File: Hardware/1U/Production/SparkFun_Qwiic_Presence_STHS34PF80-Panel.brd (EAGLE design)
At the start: 149.1 x 143.3 mm, 1306 parts, among them J1 Qwiic, J10 Qwiic, J11 Qwiic, J13 Qwiic, J14 Qwiic, J16 Qwiic, J17 Qwiic, J19 Qwiic, J2 Qwiic, J20 Qwiic, J22 Qwiic, J23 Qwiic, J25 Qwiic, J26 Qwiic, J28 Qwiic, J29 Qwiic, J31 Qwiic, J32 Qwiic, J34 Qwiic, J35 Qwiic, J37 Qwiic, J38 Qwiic, J4 Qwiic, J40 Qwiic, J41 Qwiic, J43 Qwiic, J44 Qwiic, J46 Qwiic, J47 Qwiic, J49 Qwiic, J5 Qwiic, J50 Qwiic, J52 Qwiic, J53 Qwiic, J55 Qwiic, J56 Qwiic, J58 Qwiic, J59 Qwiic, J61 Qwiic, J62 Qwiic, J64 Qwiic, J65 Qwiic, J67 Qwiic, J68 Qwiic, J7 Qwiic, J70 Qwiic, J71 Qwiic, J73 Qwiic, J74 Qwiic, J8 Qwiic, U1 STHS34PF80, U10 STHS34PF80, U11 STHS34PF80, U12 STHS34PF80, U13 STHS34PF80, U14 STHS34PF80, U15 STHS34PF80, U16 STHS34PF80, U17 STHS34PF80, U18 STHS34PF80, U19 STHS34PF80, U2 STHS34PF80, U20 STHS34PF80, U21 STHS34PF80, U22 STHS34PF80, U23 STHS34PF80, U24 STHS34PF80, U25 STHS34PF80, U3 STHS34PF80, U4 STHS34PF80, U5 STHS34PF80, U6 STHS34PF80, U7 STHS34PF80, U8 STHS34PF80, U9 STHS34PF80

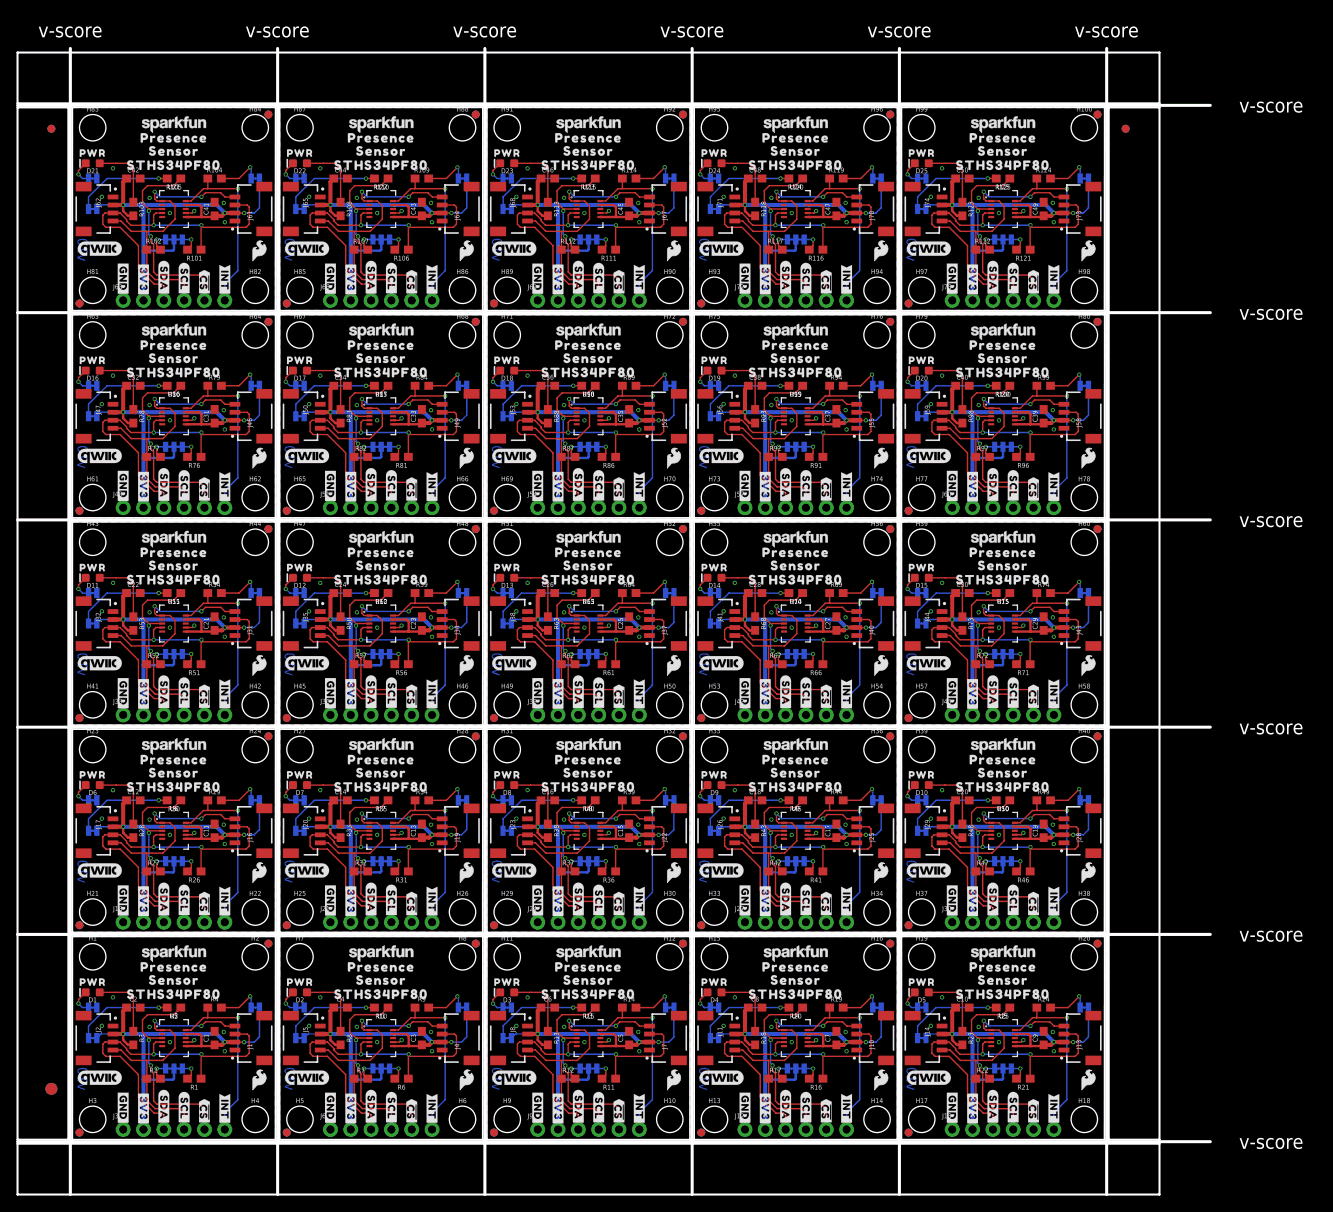
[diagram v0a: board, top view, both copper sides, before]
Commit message: Updated 1U to correct paste layer for main IC
Updated the board and the panel/gerbers to have the correct percentage of fill for the solder paste on the STHS34PF80
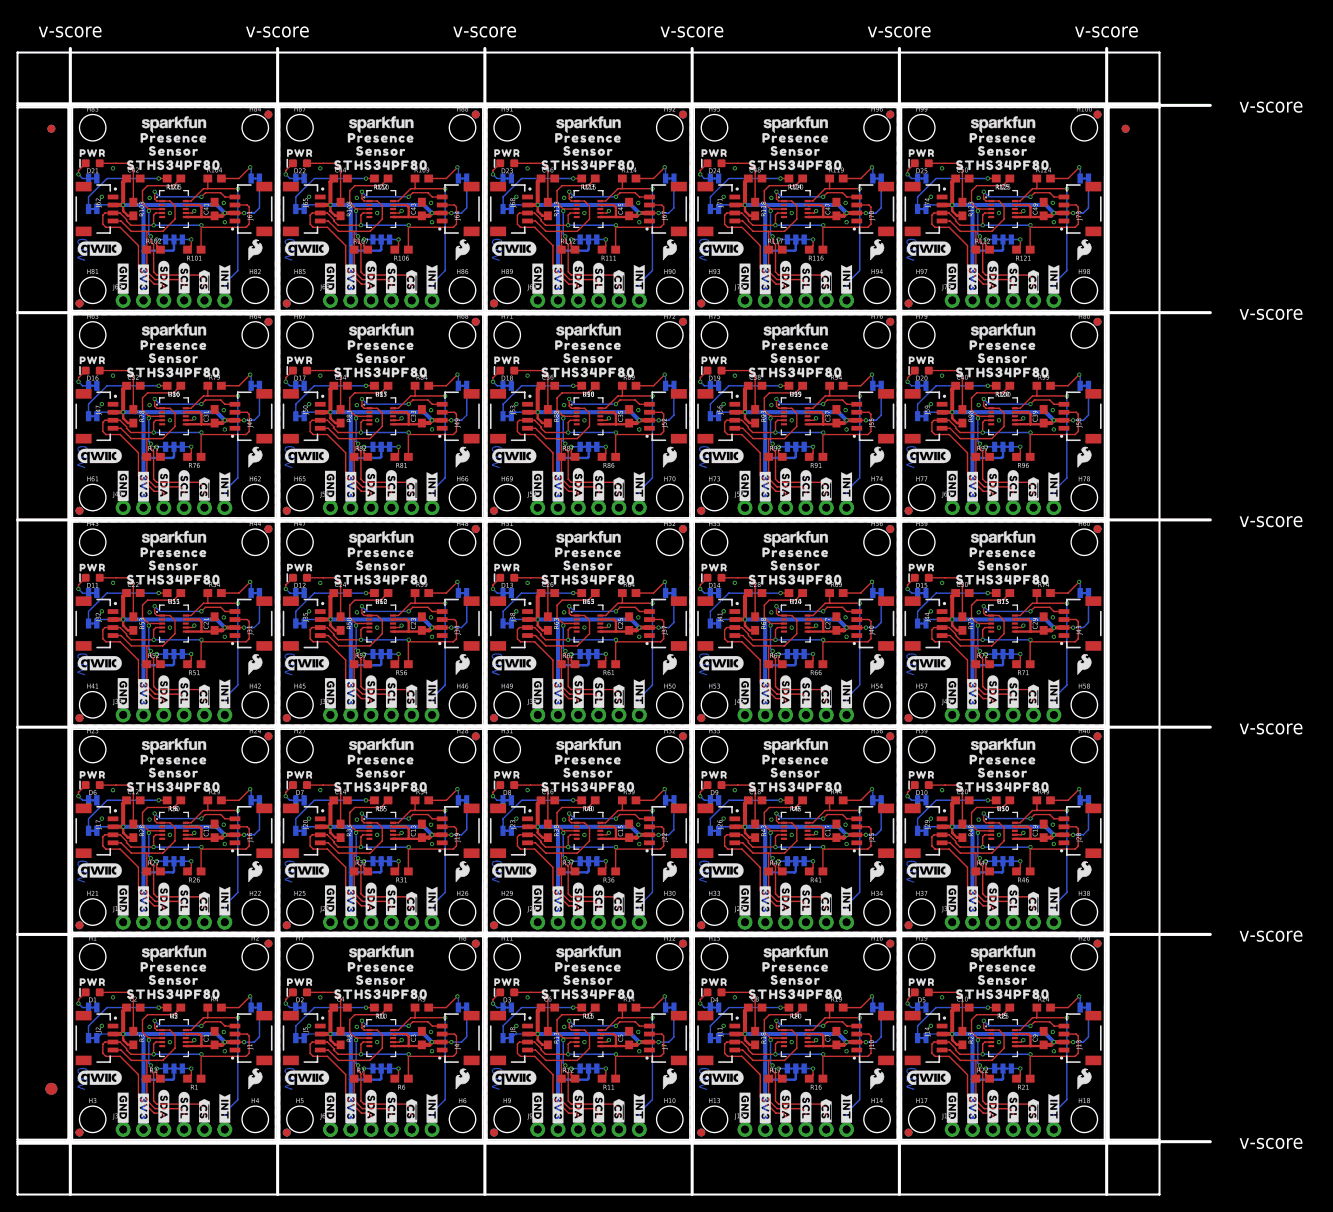
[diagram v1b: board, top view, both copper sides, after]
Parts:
- moved LOGO59 0.52 mm to (48.8, 59.4)
- moved LOGO9 0.52 mm to (48.8, 7.62)
- moved LOGO109 0.52 mm to (48.8, 111.3)
- moved LOGO34 0.52 mm to (48.8, 33.5)
- moved LOGO84 0.52 mm to (48.8, 85.3)
- moved LOGO54 0.52 mm to (22.9, 59.4)
- moved LOGO6 0.52 mm to (22.9, 7.62)
- moved LOGO104 0.52 mm to (22.9, 111.3)
- moved LOGO29 0.52 mm to (22.9, 33.5)
- moved LOGO79 0.52 mm to (22.9, 85.3)
- moved LOGO64 0.52 mm to (74.7, 59.4)
- moved LOGO69 0.52 mm to (100.6, 59.4)
- moved LOGO74 0.52 mm to (126.5, 59.4)
- moved LOGO14 0.52 mm to (74.7, 7.62)
- moved LOGO19 0.52 mm to (100.6, 7.62)
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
